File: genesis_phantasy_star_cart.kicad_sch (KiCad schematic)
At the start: 13 parts, among them J1 Sega_MegaDrive_Cart_Conn, J2 Batt, U1 315-5235, U2 MPR-11711, U3 MB8464A-15LL-SK, U4 BQ2201SN

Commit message: Add 3d model for mapper
* Added 3D model for the U1 mapper chip
* Added an extra +5v and GND via to C1 and C2.
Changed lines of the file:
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@@
 	(symbol
 		(lib_id "Graphic:Logo_Open_Hardware_Small")
-		(at 196.85 152.4 0)
+		(at 257.81 147.32 0)
 		(unit 1)
 		(exclude_from_sim yes)
@@
 		(fields_autoplaced yes)
 		(property "Reference" "#SYM1"
-			(at 196.85 145.415 0)
+			(at 257.81 140.335 0)
 			(effects
 				(font
@@
 		)
 		(property "Value" "Logo_Open_Hardware_Small"
-			(at 196.85 158.115 0)
+			(at 257.81 153.035 0)
 			(effects
 				(font
@@
 		)
 		(property "Footprint" ""
-			(at 196.85 152.4 0)
+			(at 257.81 147.32 0)
 			(effects
 				(font
@@
 		)
 		(property "Datasheet" "~"
-			(at 196.85 152.4 0)
+			(at 257.81 147.32 0)
 			(effects
 				(font
@@
 		)
 		(property "Description" "Open Hardware logo, small"
-			(at 196.85 152.4 0)
+			(at 257.81 147.32 0)
 			(effects
 				(font

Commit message: Rename mapper footprint and model
* Renamed footprint and model for mapper to be more accurate and with
  the dimentions in metric.
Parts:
- J2: now not fitted
- U1: footprint Custom:DIL42_600mil_P70mil_SmallDrill -> Custom:SPDIP-42_W15.24mm_P1.78mm
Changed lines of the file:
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@@
 			)
 		)
-		(property "Footprint" "Custom:DIL42_600mil_P70mil_SmallDrill"
+		(property "Footprint" "Custom:SPDIP-42_W15.24mm_P1.78mm"
 			(at 106.68 93.98 0)
 			(effects
@@
 		(in_bom yes)
 		(on_board yes)
-		(dnp no)
+		(dnp yes)
 		(property "Reference" "J2"
 			(at 218.694 38.608 0)

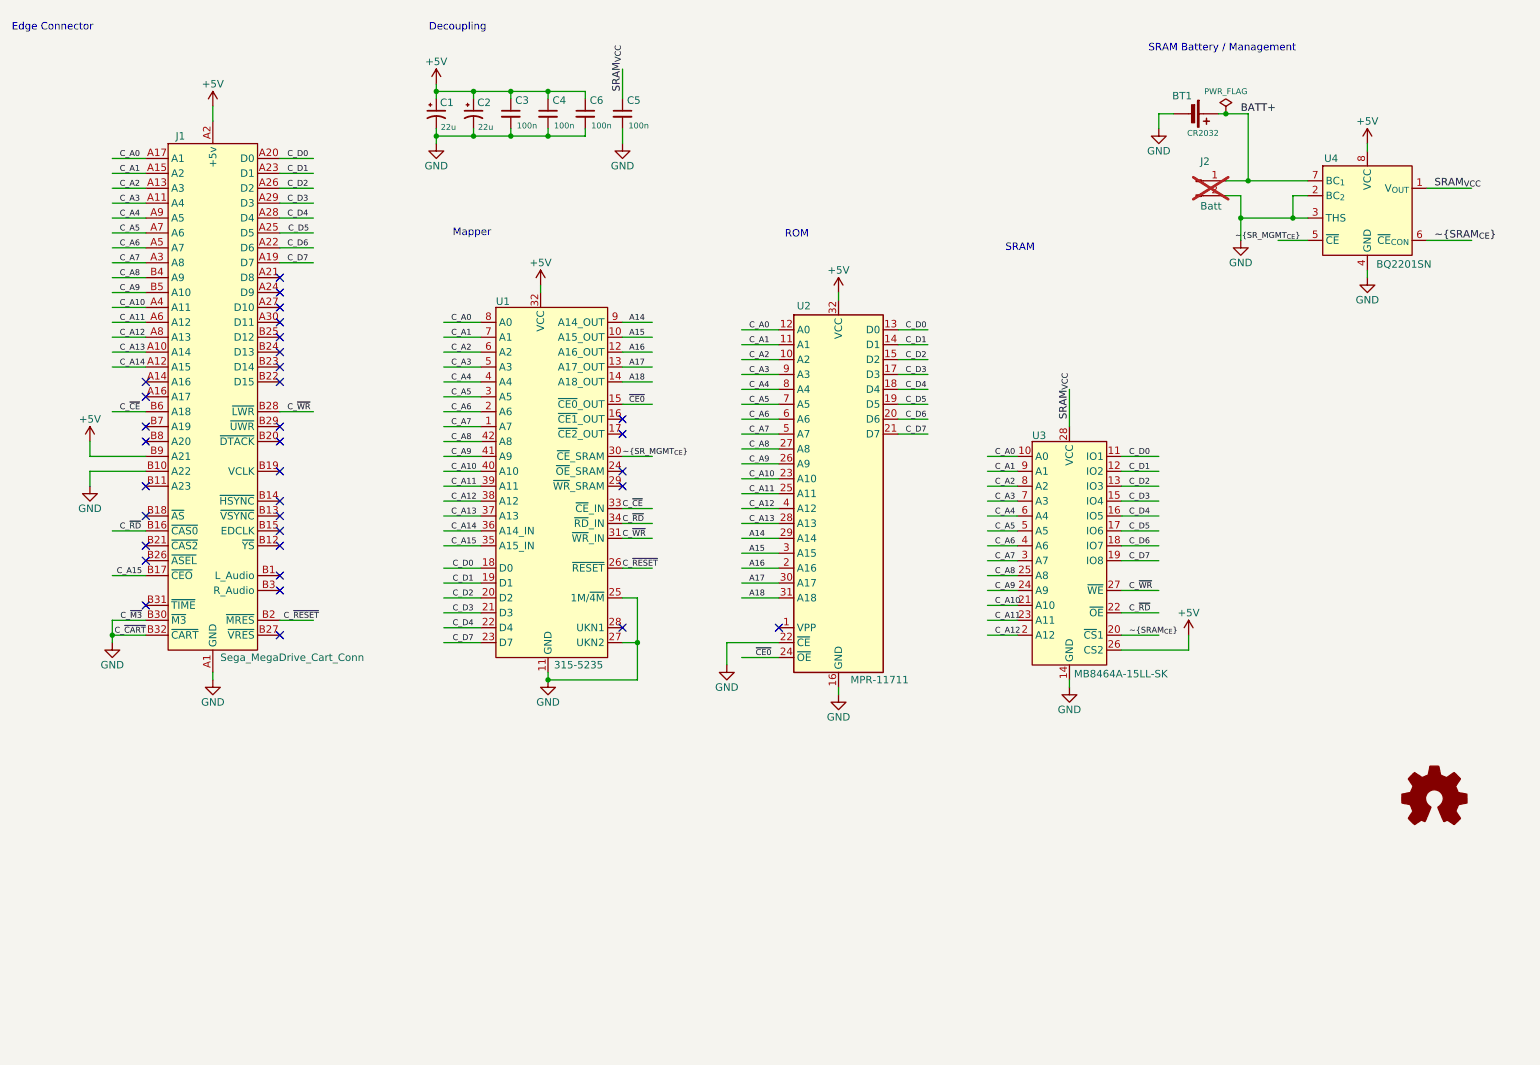
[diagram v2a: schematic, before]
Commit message: Changes leading to Rev 2 of the board
* Trimmed wings off of the edges of the board to make it a regular
  shape.
* Slightly moved around U1/2/3 to make more room around the cutouts.
* Moved backup battery connection, but remains pin headers as a CR2032
  footprint won't fit on the board with the ICs where they are.
* Enlarged drill size for U1 pads to allow the pins to fit easier.
* Various tracks nudged or rerouted to create more clearance.
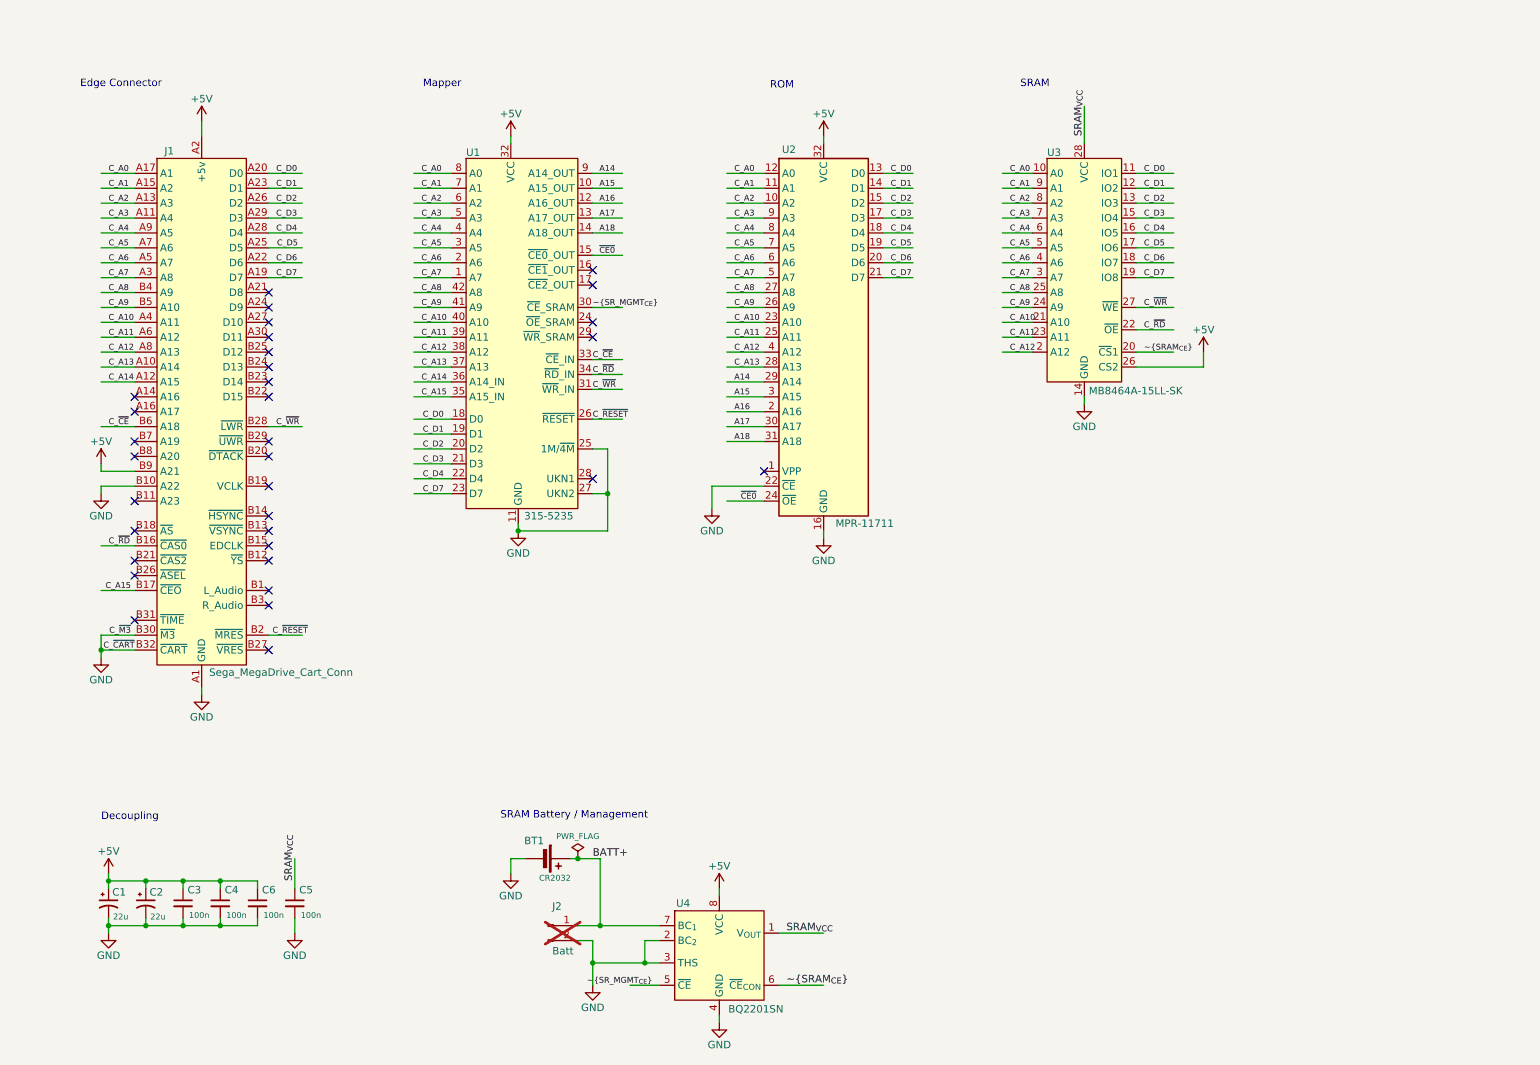
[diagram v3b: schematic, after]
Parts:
- J1: now left out of the parts list
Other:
- moved on the sheet: BT1, C1, C2, C3, C4, C5, C6, J1, J2, U1, U2, U3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

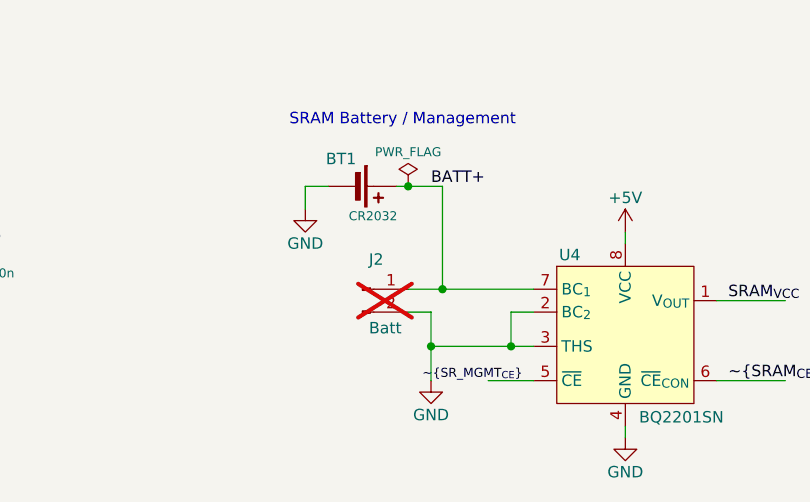
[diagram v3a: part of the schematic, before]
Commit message: Convert backup battery to proper footprint
* Backup battery is now using a proper footprint for a CR2032 with
  solder tabs. Kapton tape will be needed between battery and pins on
  the backside of the board.
* Converted battery pin header to be a secondary battery to
  maintain the SRAM while changing the primary battery. Added a pulldown
  to this to keep the supervisor happy while the seconary is not
  connected.
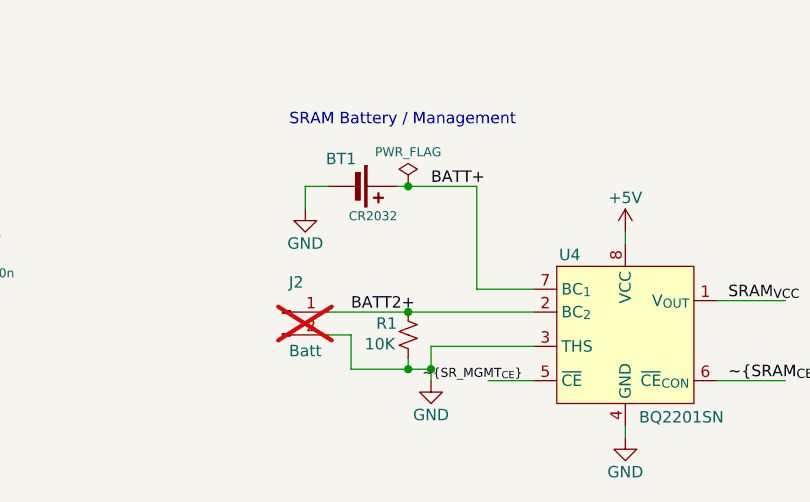
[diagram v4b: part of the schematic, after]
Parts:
- added R1: 10K, Resistor_SMD:R_0603_1608Metric, symbol Device:R_Small_US
- BT1: footprint Battery:BatteryHolder_Keystone_3002_1x2032 -> Custom:CR2032L-F1N
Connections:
- net BATT+: no longer J2.1 (Pin_1)
- net GND: now also R1.2; no longer U4.2 (BC_{2})
- new net BATT2+: J2.1 (Pin_1), R1.1, U4.2 (BC_{2})
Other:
- moved on the sheet: J2
